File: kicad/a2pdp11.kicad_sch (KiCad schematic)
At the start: 44 parts, among them J1 DCJ11A, J2 DCJ11B, J3 TN9A, J4 TN9A, J5 A2BUSA, J6 A2BUSB, J7 3V3, J8 5V, J9 Jumper, SW1 HALT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

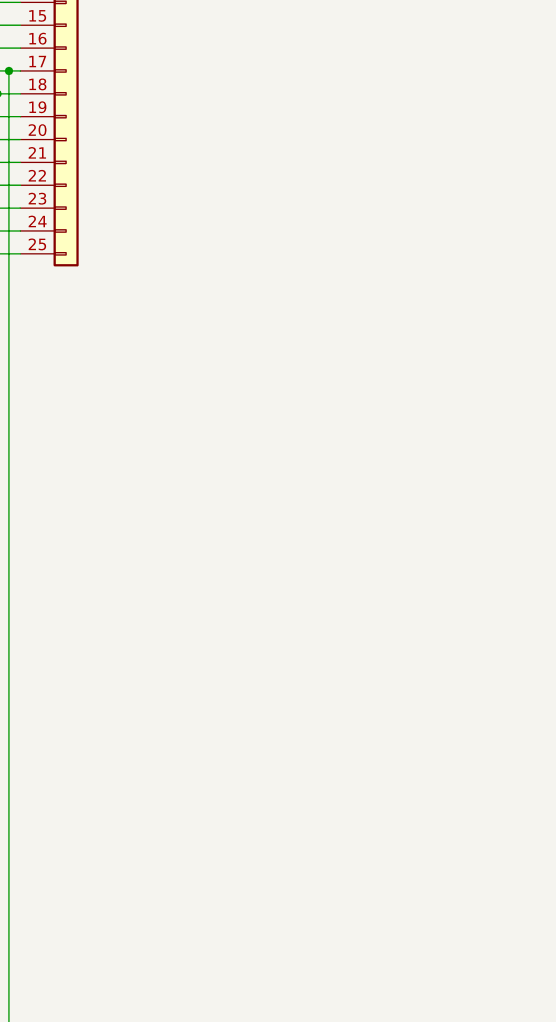
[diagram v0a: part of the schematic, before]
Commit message: PC11 paper tape reader
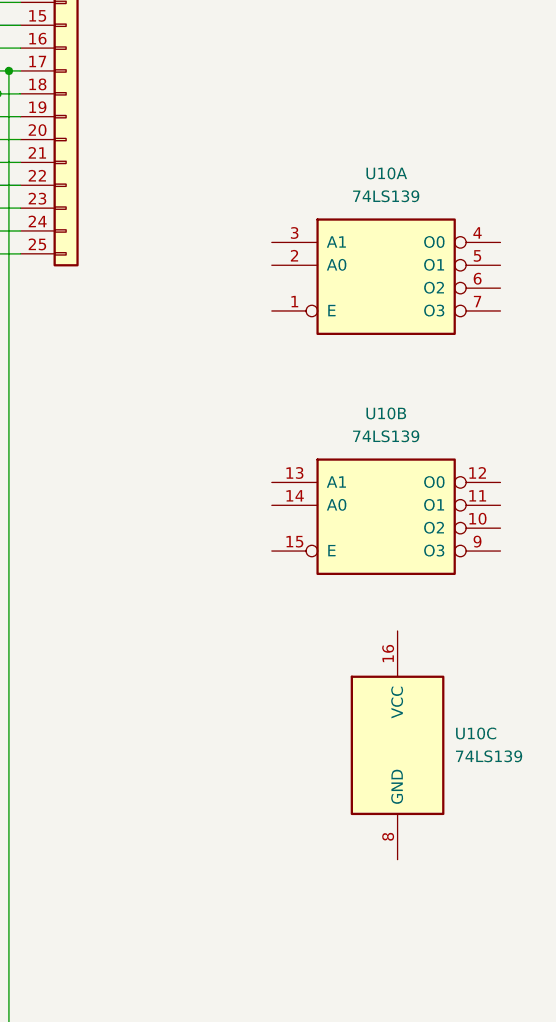
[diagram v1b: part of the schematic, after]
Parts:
- added U10: 74LS139, symbol 74xx:74LS139
